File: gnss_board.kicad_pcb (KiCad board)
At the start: 2 copper layers, 125 parts, among them J1 Conn_01x10_Pin, J2 Serial Connector, J3 U.FL, J4 Conn_01x04_Pin, Q1 BC817, Q2 BC817, T1 LMUN2211LT1G, U1 H1102NL, U2 LAN8710A, U3 TPS2375D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

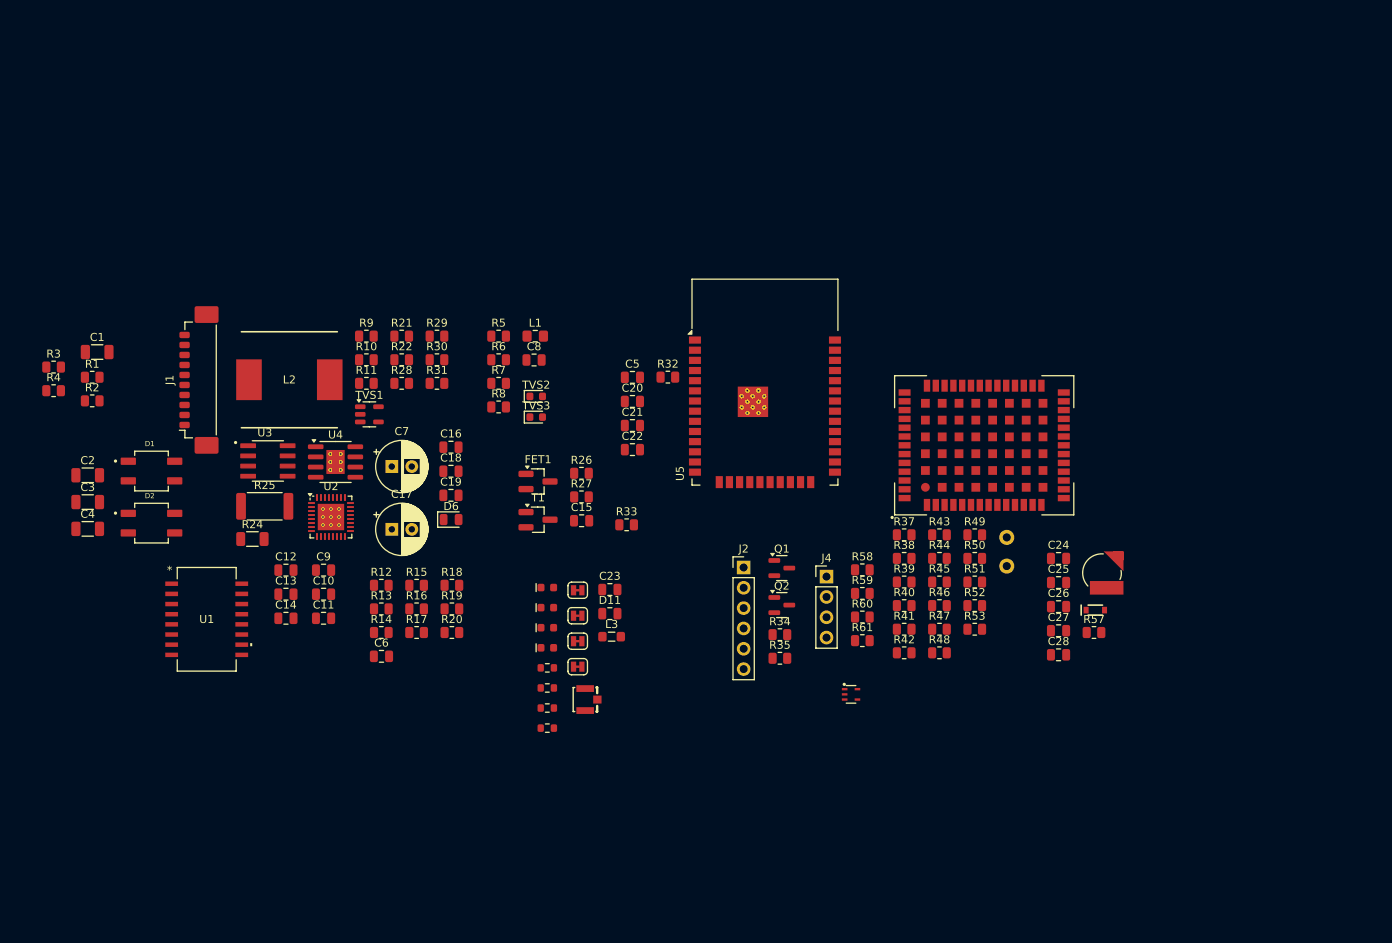
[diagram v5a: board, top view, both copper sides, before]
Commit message: PCB Edges
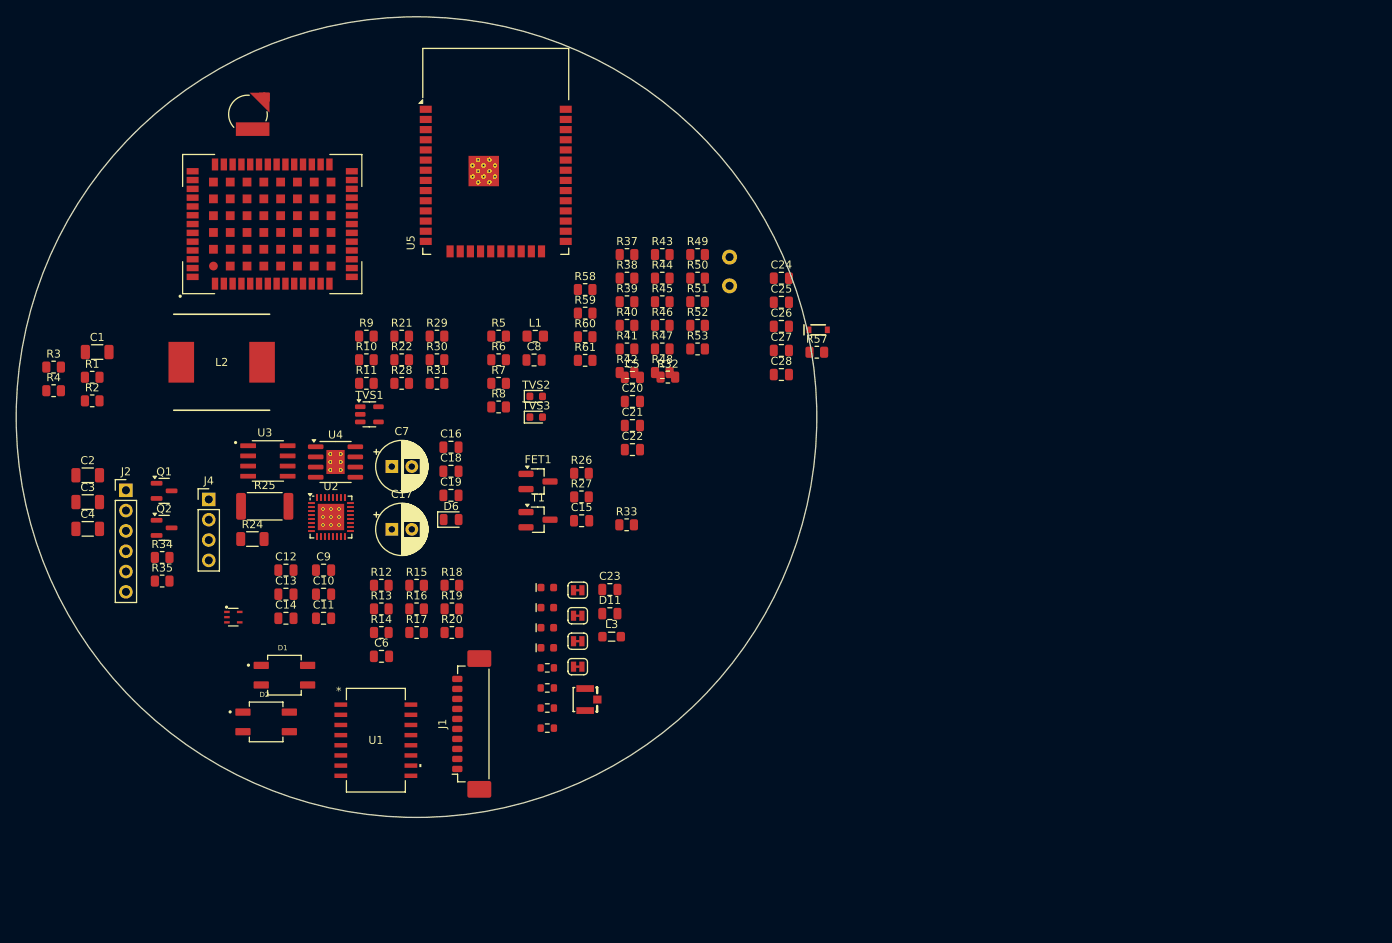
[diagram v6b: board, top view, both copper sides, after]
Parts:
- moved BT1 121.2 mm to (72.4, 40.6)
- moved U6 93.2 mm to (75.4, 54.4)
- moved J2 77.8 mm to (57.1, 87.6)
- moved D12 77.8 mm to (70.6, 103.5)
- moved J4 77.8 mm to (67.5, 88.8)
- moved Q1 77.8 mm to (61.9, 87.7)
- moved Q2 77.8 mm to (61.9, 92.3)
- moved R34 77.8 mm to (61.7, 96.0)
- moved R35 77.8 mm to (61.7, 99.0)
- moved J1 54.9 mm to (99.8, 116.8)
- moved R43 49.3 mm to (124.2, 58.2)
- moved R44 49.3 mm to (124.2, 61.1)
- moved R47 49.3 mm to (124.2, 70.0)
- moved R48 49.3 mm to (124.2, 72.9)
- moved R49 49.3 mm to (128.6, 58.2)
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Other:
- board outline added: 100.1 x 100.1 mm
- copper layers 2 -> 4

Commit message: Messing around
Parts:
- removed JP2, JP3, JP4, JP5: ~, SparkFun-Jumper:Jumper_2_NC_Trace
- removed R36, R56: 1k, SparkFun-Resistor:R_0603_1608Metric
- removed R54, R55: 2.2k, SparkFun-Resistor:R_0603_1608Metric
- removed U3: TPS2375D, GNSS Board:SOIC127P599X175-8N
- D12: footprint SparkFun-Semiconductor-Standard:SOT-353 -> Package_TO_SOT_SMD:SOT-353_SC-70-5_Handsoldering
- moved C19 120.2 mm to (211.6, 49.8)
- moved C18 111.3 mm to (207.2, 64.9)
- moved R30 99.7 mm to (189.5, 36.7)
- moved R31 99.7 mm to (189.5, 39.7)
- moved R3 84.0 mm to (131.7, 80.8)
- moved R4 83.6 mm to (131.7, 77.7)
- moved J3 82.1 mm to (68.7, 45.7)
- moved R1 79.9 mm to (131.7, 86.9)
- moved R2 79.1 mm to (131.7, 83.8)
- moved C4 76.0 mm to (127.0, 77.7)
- moved C1 75.2 mm to (127.0, 86.9)
- moved C3 75.0 mm to (127.0, 80.8)
- moved C2 74.6 mm to (127.0, 83.8)
- moved R57 71.2 mm to (72.3, 70.8)
- moved L3 63.2 mm to (54.9, 101.1)
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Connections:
- D12 pad 4: unconnected-(D12-K3-Pad4) -> ESP_RXD0
- D12 pad 5: unconnected-(D12-K4-Pad5) -> ESP_TXD0
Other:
- board size 100.1 x 100.1 mm -> 102.2 x 100.3 mm

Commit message: Moving components around
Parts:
- added D3: SS510, Diode_SMD:D_SMC_Handsoldering, F.Cu at (110.3, 60.1)
- added D5: LED, LED_SMD:LED_0805_2012Metric, F.Cu at (100.7, 110.4)
- moved L3 108.7 mm to (155.8, 141.6)
- moved R20 108.7 mm to (160.0, 111.2)
- moved R21 108.7 mm to (160.0, 114.2)
- moved R22 108.7 mm to (160.0, 117.2)
- moved R26 108.7 mm to (160.0, 120.1)
- moved R27 108.7 mm to (160.0, 123.0)
- moved R32 108.7 mm to (164.4, 108.3)
- moved R33 108.7 mm to (164.4, 111.2)
- moved R34 108.7 mm to (164.4, 114.2)
- moved R35 108.7 mm to (164.4, 117.2)
- moved R37 108.7 mm to (164.4, 120.1)
- moved R38 108.7 mm to (164.4, 123.0)
- moved R42 108.7 mm to (168.8, 105.3)
- moved R43 108.7 mm to (168.8, 108.3)
- moved R44 108.7 mm to (168.8, 111.2)
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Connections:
- D10 pad 1: (no net) -> Net-(D10-K)
- D10 pad 2: (no net) -> +3.3V
- R57 pad 2: Net-(D10-PadC) -> Net-(D10-K)
